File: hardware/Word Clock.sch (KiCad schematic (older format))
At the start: 42 parts, among them J1 UX60SC-MB-5ST(80), M1 MOUNTING-HOLE, M2 MOUNTING-HOLE, M3 MOUNTING-HOLE, M4 MOUNTING-HOLE, P1 RTC, P2 Light Sense, P3 ICSP, P4 Row, P5 Column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

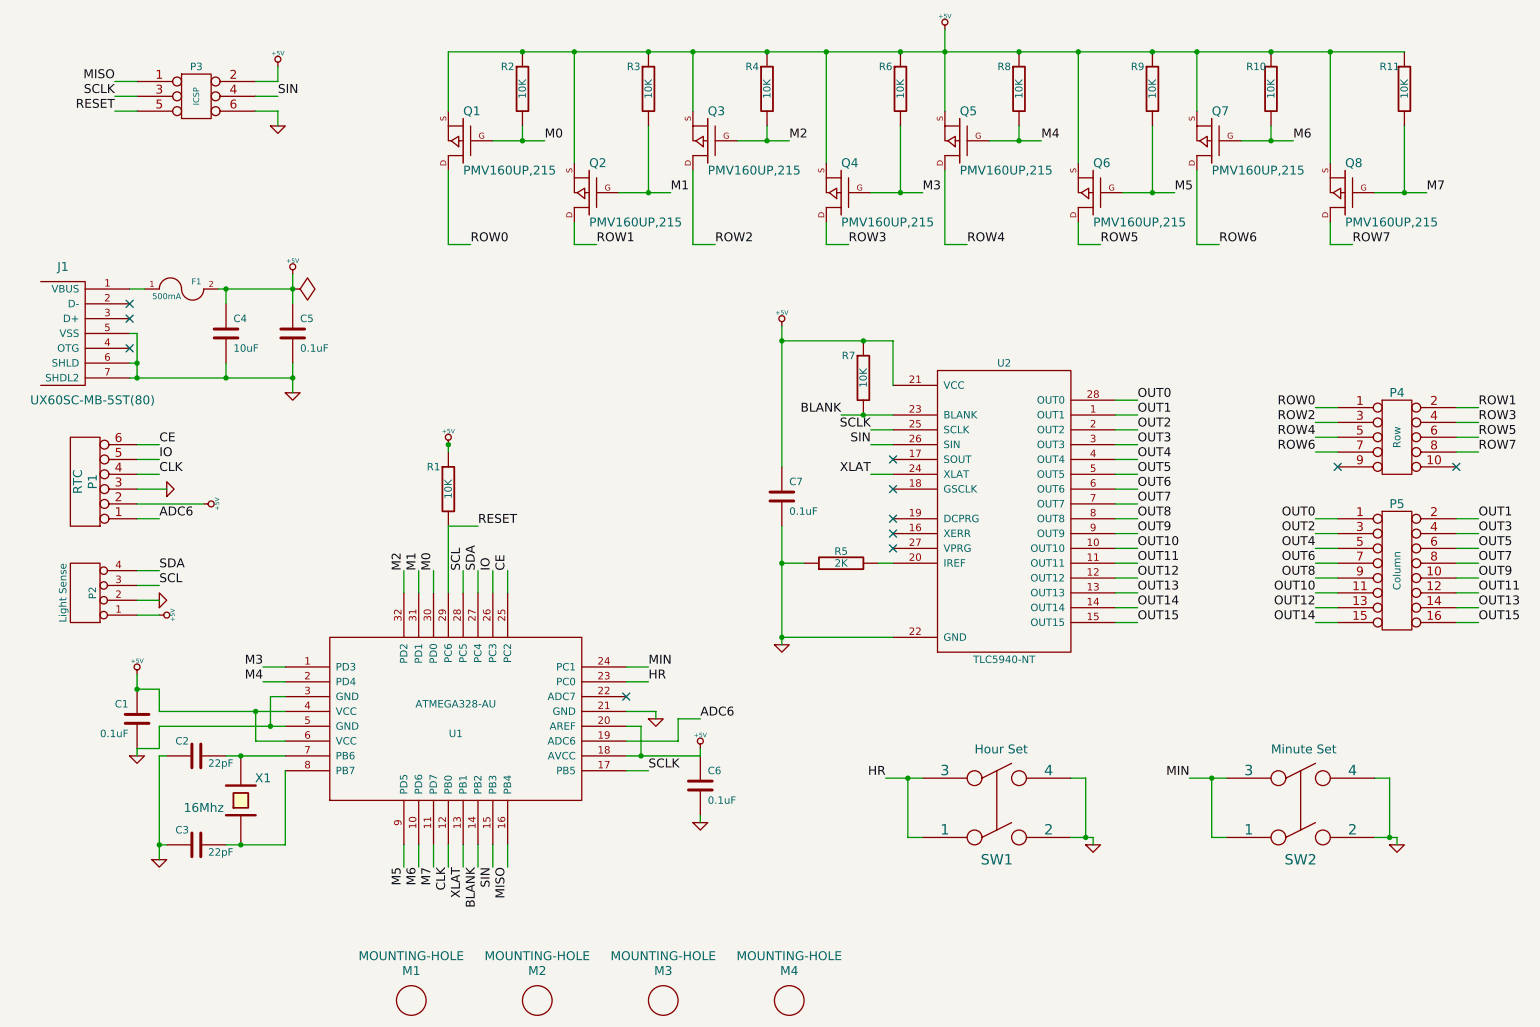
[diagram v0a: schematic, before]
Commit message: Shift Register added to sch
Since I/O was full on atmega, shift register was added for driving the 8
mosfets.
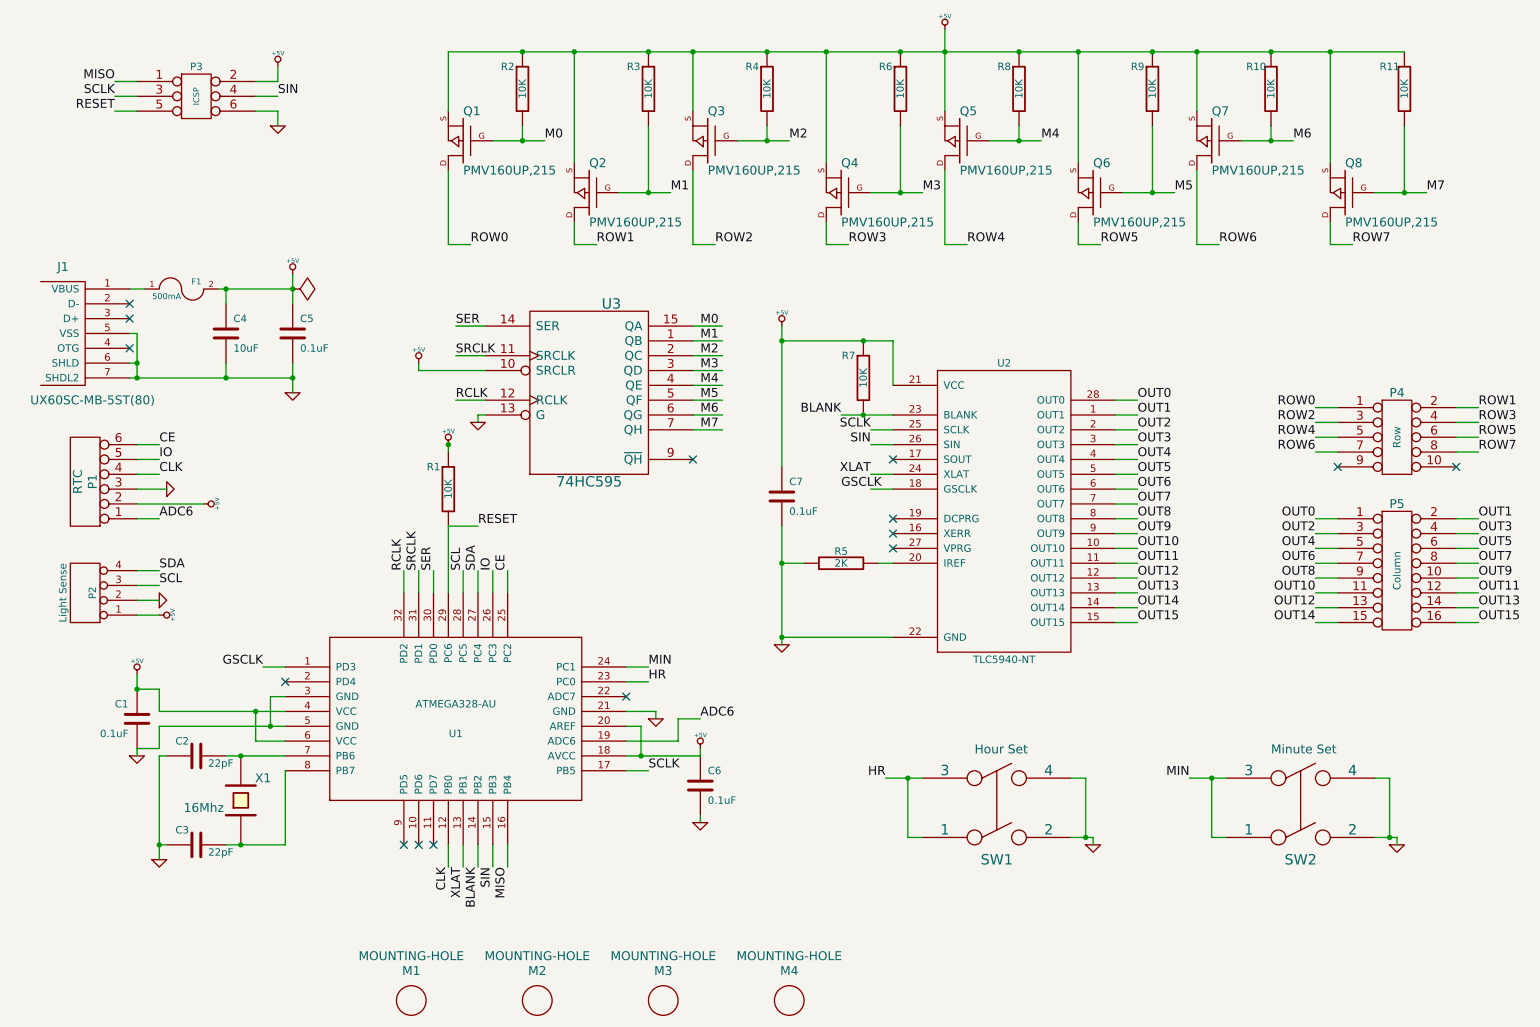
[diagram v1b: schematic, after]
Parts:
- added U3: 74HC595, ~, symbol 74HC595
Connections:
- net labels added: GSCLK, RCLK, SER, SRCLK
- wire segments 185 -> 197
- no-connect marks 11 -> 15

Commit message: Fixed TLC5940 Missing connections.
Tied VPRG to GND and DCPRG to VCC.
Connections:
- wire segments 197 -> 201
- no-connect marks 15 -> 13
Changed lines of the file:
@@
 	1    0    0    -1
 $EndComp
-NoConn ~ 6600 4300
 NoConn ~ 6600 4200
-NoConn ~ 6600 4100
 Text Label 6250 3400 2    60   ~ 0
 BLANK
@@
 NoConn ~ 3400 6300
 NoConn ~ 3500 6300
+Wire Wire Line
+	6600 4300 5850 4300
+Connection ~ 5850 4300
+Wire Wire Line
+	6600 4100 6150 4100
+Wire Wire Line
+	6150 4100 6150 3650
+Wire Wire Line
+	6150 3650 5850 3650
+Connection ~ 5850 3650
 $EndSCHEMATC
